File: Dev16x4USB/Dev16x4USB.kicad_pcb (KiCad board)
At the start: 2 copper layers, 19 parts, among them J1 USB_B_Micro, J2 Header, J3 Header, SW1 SW_Push_DPDT, U1 LM1117-3.3, U2 ATtiny16x4-SS, U3 CH340E

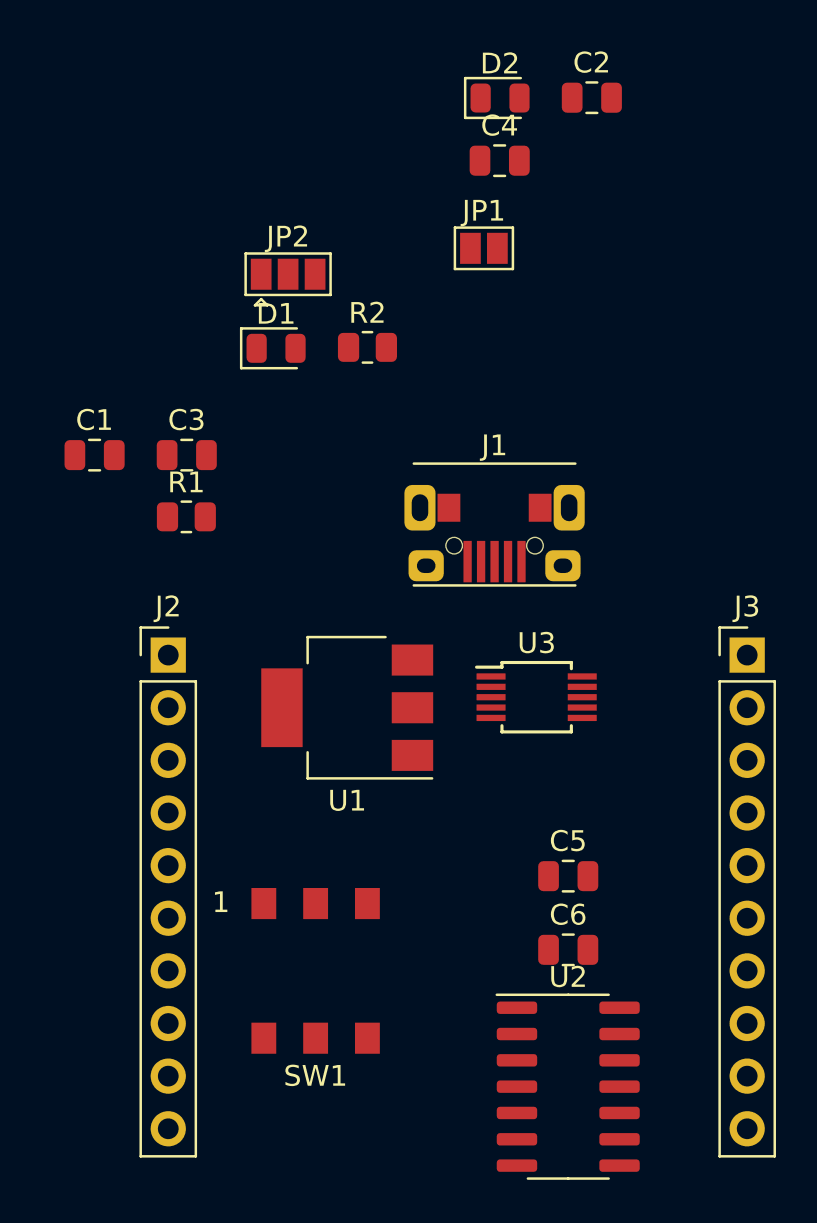
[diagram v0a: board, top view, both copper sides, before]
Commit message: Finish v1 16x4 USB
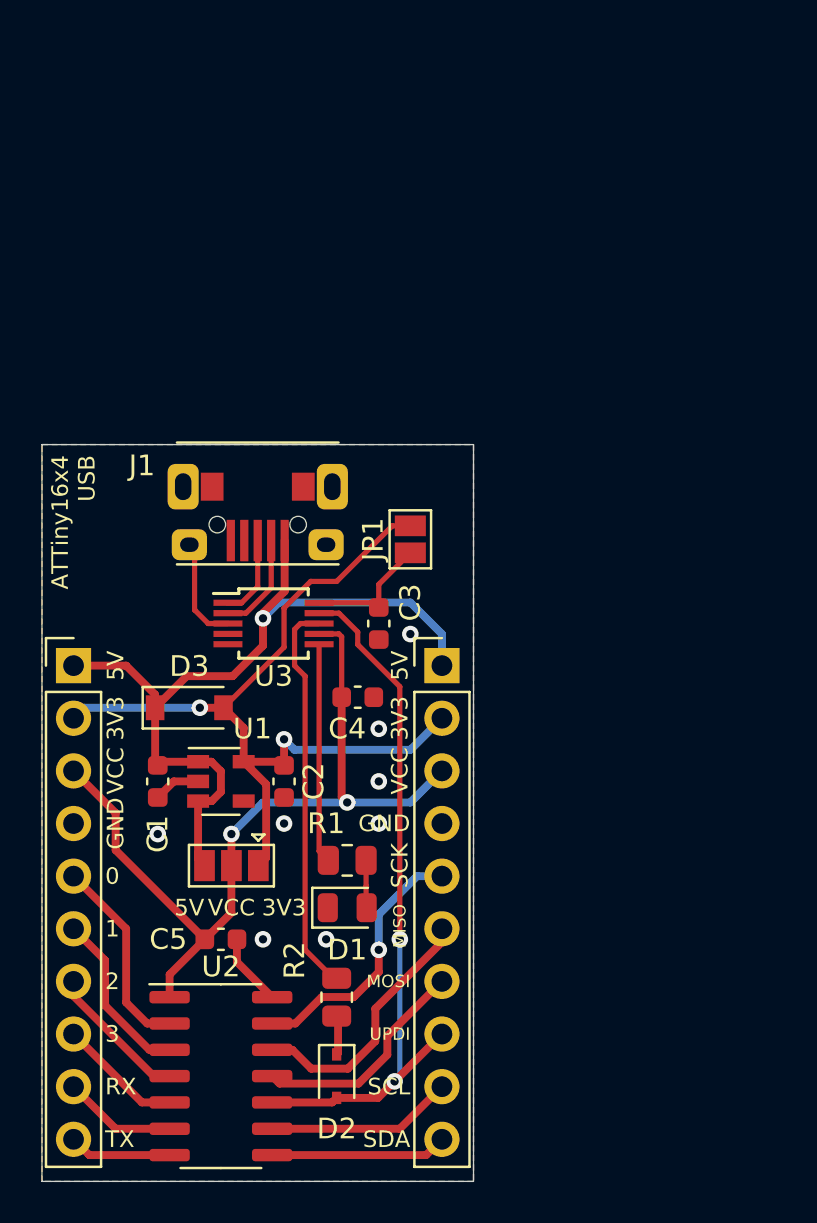
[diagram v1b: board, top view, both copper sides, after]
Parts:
- removed the C5 at (130.6, 96.5)
- removed SW1: SW_Push_DPDT, footprints:Wurth-452403012014
- added D3: MBR0520LT1G, Diode_SMD:D_SOD-123, F.Cu at (112.3, 88.4)
- added REF**: OSHW-Logo2_7.3x6mm_SilkScreen, Symbol:OSHW-Logo2_7.3x6mm_SilkScreen, B.Cu at (115.3, 108.2)
- C1, C2, C3, C4: footprint Capacitor_SMD:C_0805_2012Metric -> Capacitor_SMD:C_0603_1608Metric
- C5: renamed from C6; footprint Capacitor_SMD:C_0805_2012Metric -> Capacitor_SMD:C_0603_1608Metric
- D2: footprint Diode_SMD:D_0805_2012Metric -> Diode_SMD:D_SOD-323
- U1: value LM1117-3.3 -> LD39015M33R; footprint Package_TO_SOT_SMD:SOT-223-3_TabPin2 -> Package_TO_SOT_SMD:SOT-23-5
- moved D2 47.9 mm to (119.4, 106.2), turned to 270 degrees
- moved C2 36.2 mm to (116.8, 91.9), turned to 270 degrees
- moved R2 31.4 mm to (119.4, 102.4), turned to 90 degrees
- moved VCC 28.7 mm to (114.3, 96.0), turned to 180 degrees
- moved D1 27.2 mm to (119.9, 98.0)
- moved C4 26.8 mm to (120.4, 87.9)
- moved R1 18.3 mm to (119.9, 95.8)
- moved C5 16.8 mm to (113.8, 99.6)
- moved U2 16.8 mm to (113.8, 106.2)
- moved C1 16.0 mm to (110.7, 91.9), turned to 270 degrees
- moved J3 14.7 mm to (124.5, 86.4)
- moved JP1 14.5 mm to (122.9, 80.3), turned to 90 degrees
- moved U3 13.2 mm to (116.3, 84.3)
- moved C3 12.3 mm to (121.4, 84.3), turned to 270 degrees
- moved J1 11.5 mm to (115.6, 77.7)
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- renumbered JP2 to VCC
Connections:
- D2 pad 2: Net-(D2-Pad2) -> /UPDI
- J2 pad 10: GND -> /5_TX
- J2 pad 3: GND -> VCC
- J2 pad 4: /0_SS -> GND
- J2 pad 5: /1_VREF -> /0_SS
- J2 pad 6: /2 -> /1_VREF
- J2 pad 7: /3 -> /2
- J2 pad 8: /4_RX -> /3
- J2 pad 9: /5_TX -> /4_RX
- J3 pad 10: GND -> /6_SDA
- J3 pad 3: GND -> VCC
- J3 pad 4: /10_SCK -> GND
- J3 pad 5: /9_MISO -> /10_SCK
- J3 pad 6: /8_MOSI -> /9_MISO
- J3 pad 7: /UPDI -> /8_MOSI
- J3 pad 8: /7_SCL -> /UPDI
- J3 pad 9: /6_SDA -> /7_SCL
- R2 pad 1: /UPDI -> Net-(D2-Pad1)
- R2 pad 2: Net-(D2-Pad2) -> Net-(R2-Pad2)
- U1 pad 1: GND -> +5V
- U1 pad 2: +3V3 -> GND
- U3 pad 8: Net-(SW1-Pad2) -> Net-(R2-Pad2)
- U3 pad 9: Net-(SW1-Pad5) -> /UPDI
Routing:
- net +3V3: track 0.00 -> 41.6 mm, vias 0 -> 2
- net VCC: track 0.00 -> 40.5 mm, vias 0 -> 2
- net +5V: track 0.00 -> 39.9 mm, vias 0 -> 1
- net /UPDI: track 0.00 -> 34.4 mm, vias 0 -> 2
- net Net-(R2-Pad2): track 0.00 -> 18.9 mm
- net /10_SCK: track 0.00 -> 12.8 mm, vias 0 -> 1
- net /9_MISO: track 0.00 -> 12.7 mm
- net /8_MOSI: track 0.00 -> 10.9 mm
- net GND: track 0.00 -> 10.9 mm, vias 0 -> 8
- net Net-(R1-Pad1): track 0.00 -> 10.6 mm
- net /0_SS: track 0.00 -> 9.67 mm
- net /7_SCL: track 0.00 -> 9.03 mm
- net /6_SDA: track 0.00 -> 8.51 mm
- net /1_VREF: track 0.00 -> 8.33 mm
- net /2: track 0.00 -> 6.94 mm
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- added copper zone on B.Cu, net GND
- added copper zone on F.Cu, net GND
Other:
- board outline added: 20.8 x 35.6 mm
- board text added: "0"
- board text added: "0(SS)"
- board text added: "1"
- board text added: "1(VREF)"
- board text added: "10(SCK)"
- board text added: "11(UPDI)"
- board text added: "2"
- board text added: "3"
- board text added: "3V3"
- board text added: "4(RX)"
- board text added: "5(TX)"
- board text added: "5V"
- board text added: "6(SDA)"
- board text added: "7(SCL)"
- board text added: "8(MOSI)"
- board text added: "9(MISO)"
- board text added: "ATTiny16x4 USB"
- board text added: "ATTiny16x4 USB Dev No debug v1"
- board text added: "Designed by Alan H."
- board text added: "GND"
- board text added: "MISO"
- board text added: "MOSI"
- board text added: "RX"
- board text added: "SCK"
- board text added: "SCL"
- board text added: "SDA"
- board text added: "TX"
- board text added: "UPDI"
- board text added: "VCC"
